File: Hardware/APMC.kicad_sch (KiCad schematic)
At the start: 161 parts, among them J1 Pin header Male 2x7 P:1.27, J10 +3.3V, J11 +3.3V, J13 +3.3V, J14 Conn_01x04, J2 USB-C, J5 Terminal 1x5 P:3.5mm, J6 Terminal 1x5 P:3.5mm, J7 Terminal 1x5 P:3.5mm, J8 Conn_01x04, J9 Conn_01x04, M1 Logo_Open_Hardware_Small, Q1 DMP6023LE, Q10 BSS123, Q2 DMP6023LE, Q3 DMP6023LE, Q4 BSS123, Q5 DMP6023LE, Q6 DMP6023LE, Q7 BSS123, Q8 DMP3056L, Q9 BSS123, U1 LMR516xx, U10 TXU0202, U12 LM74703/LM74704, U13 TPS62162DSG, U2 LCFE201202A, U3 TXU0202, U4 M95P32, U5 STM32U575CITx, U6 XTR200, U7 TPS7A2031PDBVR, U8 XTR200, U9 ADS1x2S14, X1 SiT8008Bx-7x, Y1 32.768kHz

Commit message: BOM revised
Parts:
- BT1: Notes order from Farnell, DigiKey, eBay or Aliexpress -> (none); Source (none) -> in EU order from Farnell, DigiKey, eBay or AliExpress
- BTN2, H1, H2, H3, H4, J3, J4, J8, J9, M1: now left out of the parts list
- D10: Mfg MCC: BAT46WSHE3-TP -> Diotec: BAT46WS; Mouser 833-BAT46WSHE3-TP -> 637-BAT46WS; Notes 100V, 150mA -> (none)
- D4: Alt (none) -> NXP: PZU3.6B2A,115, Vishay: NXP: BZX384B3V6-*; Mfg OnSemi: MM3Z10VST1G -> NXP: PZU3.6B2A,115; Mouser 863-MM3Z10VST1G -> 771-PZU3.6B2A,115
- D5, D9: Mfg NXP:BZT52H-B10,115 -> NXP: PDZ10BF; Mouser 2069415 -> 771-PDZ10BF
- D6: Alt BAT46WJF, BAT46WSHE3-TP, GSBAT46WS, NSR02100HT1G -> BAT46WS, BAT46WJF, BAT46WSHE3-TP, GSBAT46WS, NSR02100HT1G; Mfg MCC: BAT46WSHE3-TP -> Diotec: BAT46WS; Mouser 833-BAT46WSHE3-TP -> 637-BAT46WS; Notes 100V, 150mA -> (none)
- D8: Alt (none) -> OnSemi: MM3Z3V3ST1G, NXP: PZU3.3B2A,115; Mfg NXP: PDZ3.3B,115 -> OnSemi: MM3Z3V3ST1G; Mouser 771-PDZ33B7115 -> 863-MM3Z3V3ST1G
- Di1: value Display -> LCD 240x280 1.69"; Mfg (none) -> ?; Source Aliexpress, eBay, Allegro etc. -> e.g. https://aliexpress.com/item/1005009710952964.html, htt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
- ENC1: Bourns PEC11R-4120K-S0018 (18 dents), PEC11R-4320K-S0012 (12 dents) -> PEC11R-4215K-S0024 (24 dent), PEC11R-4315K-S0012 (12 dent); Mouser 652-PEC11R4120KS0018 -> 652-PEC11R-4215K-S24; Remarks shaft 20mm Knurled, with switch, number of dents = number o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 -> base hight 6.5mm, shaft 15mm Knurled, with switch, number o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; Remarks2 PEC11R4 requires standofs 6.5 mm -> (none); now left out of the parts list
- ENC2: Mfg CUI: RIC11-31S10K2-GSMT -> CUI: RIC11-22S11K5S-USMT; Mouser 179-RIC1131S10K2GSMT -> 179-RIC122S11K5SUSMT; Remarks (none) -> base height: 4.5, mm, shaft: 10.5mm (15 mm total); now in the parts list
- J10, J11, J13: value +3.3V -> Conn_01x03
- J12: value (none) -> Conn_02x08
- J2: value USB-C -> USB-C receptacle; Alt GCT: USB4105-GF-A, Molex: 17179-0001, AMP: 10155435-00011LF -> GCT: USB4105-GF-A-120, Molex: 17179-0001, AMP: 10155435-000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; Mfg (none) -> GCT: USB4105-GF-A; Mouser (none) -> 640-USB4105-GF-A-120
- J5, J6, J7: Alt (none) -> AdamTech: EBWA-05-A, GCT: TAD05-05-1-L-G, TE:1546551-5, Pho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; Angle55 GCT: TBD05-04-1-G-G, Phoenix: 1751112, Wurth: 691221120004,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 -> (none); Mfg Phoenix: 5430027 -> AdamTech: EBWA-05-A; Mouser 651-5430027 -> 737-EBWA-05-A; Vertical TE:1546551-4, Phoenix:5430027, Eaton: EM392304 -> (none)
- Q10, Q4, Q7, Q9: Alt (none) -> Toshiba: SSM3K7002CFU,LF, NXP: NX138BKWX, DiodesInc: DMN62D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; Mfg DiodesInc: BSS123W-7-F -> Toshiba: SSM3K7002CFU,LF; Mouser 621-BSS123W-F -> 757-SSM3K7002CFULF
- Q2, Q3, Q5, Q6: Alt (none) -> MCC: MCT090P10L-TP
- R1, R2: Mfg Yageo: RT0603DRE075K1L -> Susumu: RR0816P-512-D; Mouser 603-RT0603DRE075K1L -> 754-RR0816P-512D
- R19: Mfg Susumu: RG1608P-512-D-T5 -> Susumu: RR0816P-512-D; Mouser 754-RG1608P-512DT5 -> 754-RR0816P-512D
- R20, R27, R32, R34: R R1 -> (none)
- R28: value 300k -> 681k; Mfg Panasonic: ERA-3AEB304V -> Yageo: RT0603BRD07681KL; Mouser 667-ERA-3AEB304V -> 603-RT0603BRD07681KL
- R33: value 300k -> 1.5M; Mfg Panasonic: ERA-3AEB304V -> Vishay: MCT0603MD1504BP500; Mouser 667-ERA-3AEB304V -> 594-MCT0603MD1504BP5
- R35: value 300k -> X; Mfg Panasonic: ERA-3AEB304V -> (none); Mouser 667-ERA-3AEB304V -> (none); now not fitted; now left out of the parts list
- R42: Remarks (none) -> 1%
- R6: Mfg Yageo: RT0603DRE10100KL -> Susumu: RG1608P-104-D-T5; Mouser 603-RT0603DRE10100KL -> 754-RG1608P-104DT5
- S1, S2, S3: value Jumper_2.0 -> Shunt P: 2.0 mm
- U13: Mfg TPS62162DSGR -> TI: TPS62162DSGR
- U4: Alt2 (none) -> M95P32-IXMNT, Package_SO:SO-8_3.9x4.9mm_P1.27mm (better ava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
- U6, U8: Mfg (none) -> TI: XTR200DQCR; Mouser (none) -> 595-XTR200DQCR
- U9: Alt TI: ADS122S14 (24-bit version, pin compatible) -> 24-bit pin-compatible version TI: ADS122S14, Mouser: 595-AD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; Mfg (none) -> TI: ADS112S14IRTER; Mgf TI: ADS112S14IRTER -> (none)
- Y1: Alt (none) -> ECS-.327-CDX-1128, ECS-.327-6-34RR-TR, ECS-.327-CDX-1128, E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; Notes see ST AN2867 for more options -> refer to ST document AN2867 for more options; ST reccomended ECS-.327-CDX-1128, ECS-.327-6-34RR-TR, ECS-.327-CDX-1128, E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 -> (none)
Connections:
- net SW: now reaches C20.1, L1.1, U1.6 (SW)
- no-connect marks 10 -> 18
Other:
- note added: "AWG 16-30"
- note added: "Select R21, R28, R33, and R35 according to the required input range. E.g. use a 300 kΩ, 681 kΩ, or 1.5 MΩ resistor for the 65 V, 30 V, and 15 V ranges, respectively."
- note removed: "Select R21, R28, R33, and R35 according to the required input range. E.g. use a 300 kΩ, 681 kΩ, or 2.5 MΩ resistor for the 65 V, 30 V, and 10 V ranges, respectively."
- moved on the sheet: C18, C46, D10, D13, J6, Q6, R17, R38, R40, U8

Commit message: schematic fix
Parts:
- Q1: symbol Transistor_FET:ZXMP4A16G -> Transistor_FET:BSP89; Alt MCC: MCT090P10L-TP -> TSMC: TSM950N10CW RPG; Mfg DiodesInc: DMP6023LE-13 -> OnSemi: FDT86102LZ; Mouser 621-DMP6023LE-13 -> 512-FDT86102LZ; Remarks any P-CH SOT-223-3 Mosfet with Vgs(th)max<2V, Vds>60V, Id>5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 -> any N-CH SOT-223-3 Mosfet with Vgs(th)max<2V, Vds>70V, Id>5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
- Q8: Note (none) -> consider using LM66100 in SC-70-6 pkg instead
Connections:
- net VCC: now also Q1.2 (D); no longer Q1.3 (S)
- net VIN: now also Q1.3 (S); no longer Q1.2 (D)
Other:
- moved on the sheet: Q1
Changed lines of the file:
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@@
 			)
 		)
-		(property "Angle55" ""
-			(at 106.68 30.48 0)
-			(hide yes)
-			(show_name no)
-			(do_not_autoplace no)
-			(effects
-				(font
-					(size 1.27 1.27)
-				)
-			)
-		)
-		(property "Vertical" ""
-			(at 106.68 30.48 0)
-			(hide yes)
-			(show_name no)
-			(do_not_autoplace no)
-			(effects
-				(font
-					(size 1.27 1.27)
-				)
-			)
-		)
-		(property "AliExpress" ""
-			(at 106.68 30.48 0)
-			(hide yes)
-			(show_name no)
-			(do_not_autoplace no)
-			(effects
-				(font
-					(size 1.27 1.27)
-				)
-			)
-		)
-		(property "Source" ""
-			(at 106.68 30.48 0)
-			(hide yes)
-			(show_name no)
-			(do_not_autoplace no)
-			(effects
-				(font
-					(size 1.27 1.27)
-				)
-			)
-		)
-		(property "ST reccomended" ""
+		(property "Note" "consider using LM66100 in SC-70-6 pkg instead"
 			(at 106.68 30.48 0)
 			(hide yes)
@@
 	)
 	(symbol
-		(lib_id "Transistor_FET:ZXMP4A16G")
-		(at 33.02 27.94 90)
+		(lib_id "Transistor_FET:BSP89")
+		(at 33.02 27.94 270)
+		(mirror x)
 		(unit 1)
 		(body_style 1)
@@
 		(dnp no)
 		(property "Reference" "Q1"
-			(at 36.576 29.21 90)
+			(at 35.052 28.956 90)
 			(show_name no)
 			(do_not_autoplace no)
@@
 					(size 1.27 1.27)
 				)
+				(justify left)
 			)
 		)
@@
 		)
 		(property "Footprint" "Package_TO_SOT_SMD:SOT-223-3_TabPin2"
-			(at 34.925 22.86 0)
+			(at 31.115 22.86 0)
 			(hide yes)
 			(show_name no)
@@
 		)
 		(property "Datasheet" ""
-			(at 33.02 27.94 0)
+			(at 29.21 22.86 0)
 			(hide yes)
 			(show_name no)
@@
 			)
 		)
-		(property "Mouser" "621-DMP6023LE-13"
+		(property "Mouser" "512-FDT86102LZ"
 			(at 33.02 27.94 0)
 			(hide yes)
@@
 			)
 		)
-		(property "Mfg" "DiodesInc: DMP6023LE-13"
+		(property "Mfg" "OnSemi: FDT86102LZ"
 			(at 33.02 27.94 0)
 			(hide yes)
@@
 			)
 		)
-		(property "Remarks" "any P-CH SOT-223-3 Mosfet with Vgs(th)max<2V, Vds>60V, Id>5A, low Rds(on)"
+		(property "Remarks" "any N-CH SOT-223-3 Mosfet with Vgs(th)max<2V, Vds>70V, Id>5A, low Rds(on)"
 			(at 33.02 27.94 90)
 			(hide yes)
@@
 			)
 		)
-		(property "Alt" "MCC: MCT090P10L-TP"
+		(property "Alt" "TSMC: TSM950N10CW RPG"
 			(at 33.02 27.94 90)
 			(hide yes)

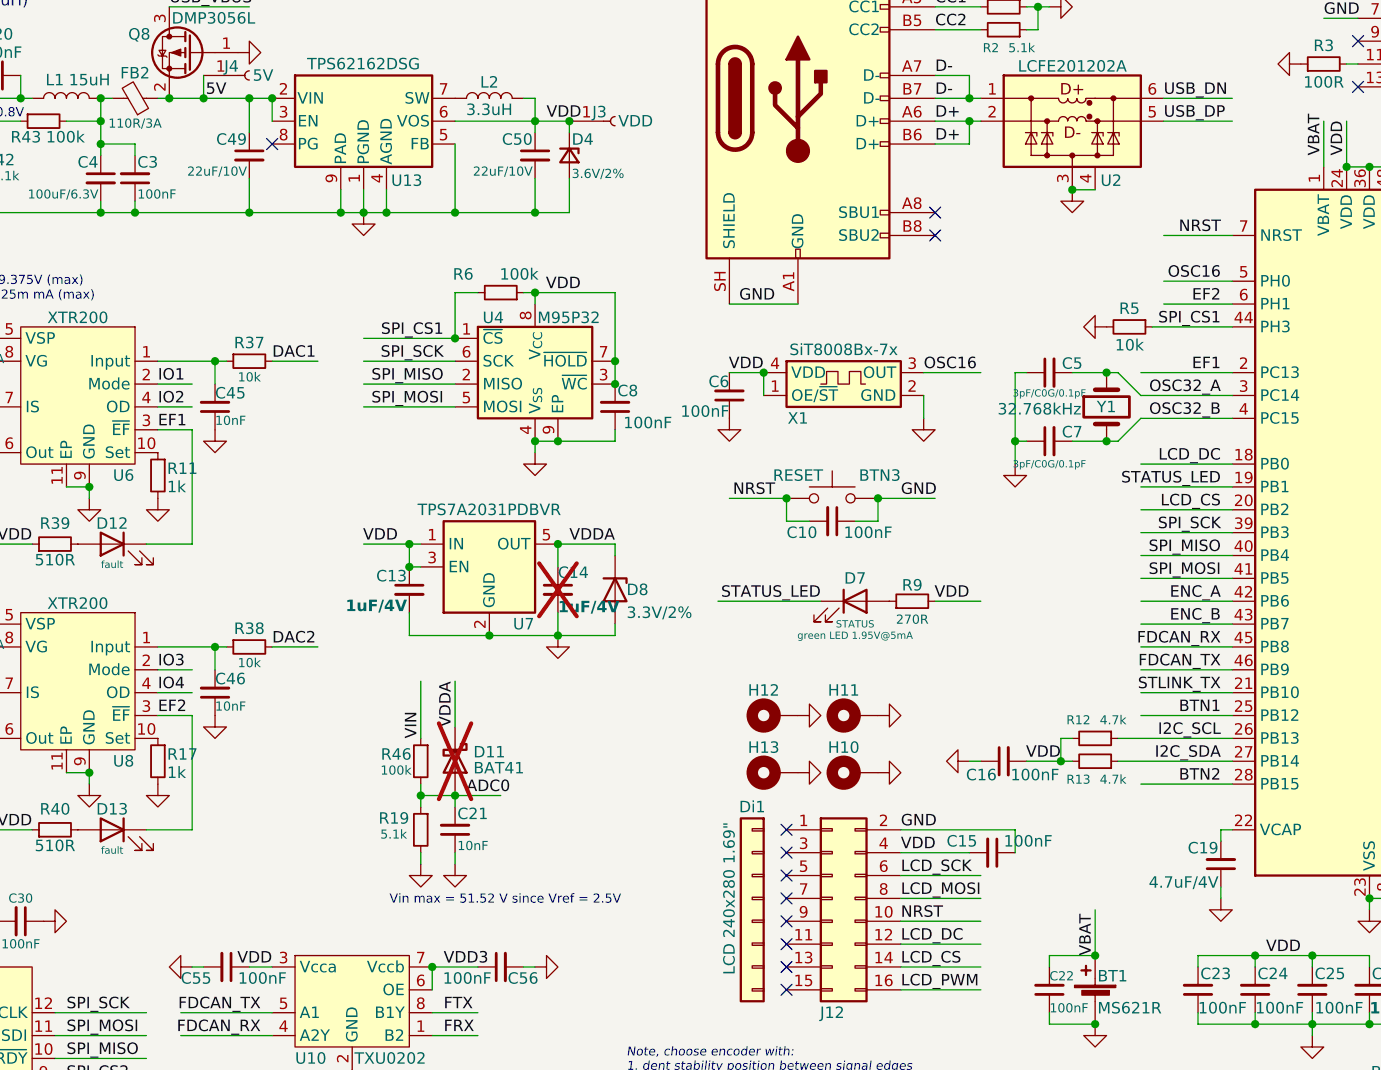
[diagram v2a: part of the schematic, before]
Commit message: R19 fix
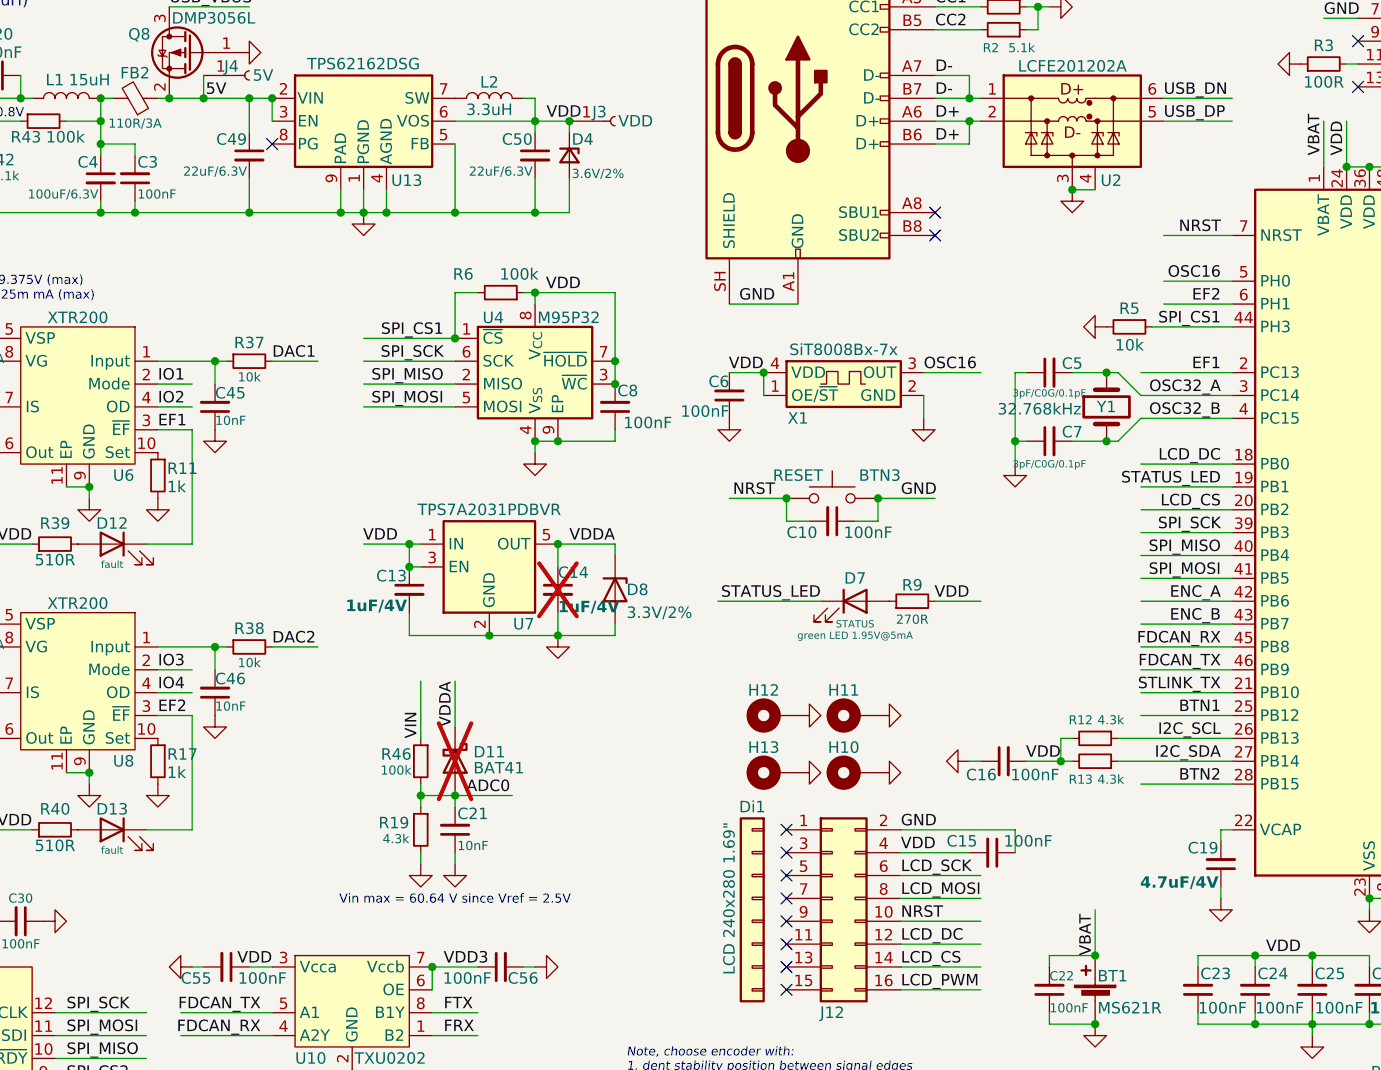
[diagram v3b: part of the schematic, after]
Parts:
- C49, C50: value 22uF/10V -> 22uF/6.3V
- Q10, Q9: Notes Vds 80V min, Vgs(th) ~1.5V, Rds(on) ≤ 10Ω -> Vds(max) ≥ 30V, Vgs(th) ~1.5V, Vgs(max) ≥ ±20V, Rds(on) ≤ 1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
- R12, R13: value 4.7k -> 4.3k; Mfg Susumu: RG1608P-472-D-T5 -> Susumu: RR0816P-432-D; Mouser 754-RG1608P-472DT5 -> 754-RR0816P-432D
- R19: value 5.1k -> 4.3k; Mfg Susumu: RR0816P-512-D -> Susumu: RR0816P-432-D; Mouser 754-RR0816P-512D -> 754-RR0816P-432D
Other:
- note added: "Vin max = 60.64 V since Vref = 2.5V"
- note removed: "Vin max = 51.52 V since Vref = 2.5V"
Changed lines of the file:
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@@
 		)
 	)
-	(text "Vin max = 51.52 V since Vref = 2.5V"
+	(text "Vin max = 60.64 V since Vref = 2.5V"
 		(exclude_from_sim no)
-		(at 141.478 124.714 0)
+		(at 135.89 124.714 0)
 		(effects
 			(font
@@
 	(wire
 		(pts
-			(xy 135.89 113.03) (xy 140.97 113.03)
+			(xy 135.89 113.03) (xy 142.24 113.03)
 		)
 		(stroke
@@
 		(dnp no)
 		(property "Reference" "R19"
-			(at 130.81 115.57 0)
+			(at 130.81 116.078 0)
 			(show_name no)
 			(do_not_autoplace no)
@@
 			)
 		)
-		(property "Value" "5.1k"
-			(at 130.556 117.348 0)
+		(property "Value" "4.3k"
+			(at 130.81 117.856 0)
 			(show_name no)
 			(do_not_autoplace no)
@@
 			)
 		)
-		(property "Mfg" "Susumu: RR0816P-512-D"
+		(property "Mfg" "Susumu: RR0816P-432-D"
 			(at 132.08 116.84 0)
 			(hide yes)
@@
 			)
 		)
-		(property "Mouser" "754-RR0816P-512D"
+		(property "Mouser" "754-RR0816P-432D"
 			(at 132.08 116.84 0)
 			(hide yes)
@@
 			)
 		)
-		(property "Value" "22uF/10V"
+		(property "Value" "22uF/6.3V"
 			(at 144.526 43.688 0)
 			(show_name no)
@@
 		(dnp no)
 		(property "Reference" "R13"
-			(at 206.502 111.252 90)
+			(at 206.756 111.252 90)
 			(show_name no)
 			(do_not_autoplace no)
@@
 			)
 		)
-		(property "Value" "4.7k"
-			(at 207.518 111.252 90)
+		(property "Value" "4.3k"
+			(at 207.264 111.252 90)
 			(show_name no)
 			(do_not_autoplace no)
@@
 			)
 		)
-		(property "Mfg" "Susumu: RG1608P-472-D-T5"
+		(property "Mfg" "Susumu: RR0816P-432-D"
 			(at 207.01 109.22 0)
 			(hide yes)
@@
 			)
 		)
-		(property "Mouser" "754-RG1608P-472DT5"
+		(property "Mouser" "754-RR0816P-432D"
 			(at 207.01 109.22 0)
 			(hide yes)
@@
 		(dnp no)
 		(property "Reference" "R12"
-			(at 206.502 104.648 90)
+			(at 206.756 104.648 90)
 			(show_name no)
 			(do_not_autoplace no)
@@
 			)
 		)
-		(property "Value" "4.7k"
-			(at 207.518 104.648 90)
+		(property "Value" "4.3k"
+			(at 207.264 104.648 90)
 			(show_name no)
 			(do_not_autoplace no)
@@
 			)
 		)
-		(property "Mfg" "Susumu: RG1608P-472-D-T5"
+		(property "Mfg" "Susumu: RR0816P-432-D"
 			(at 207.01 106.68 0)
 			(hide yes)
@@
 			)
 		)
-		(property "Mouser" "754-RG1608P-472DT5"
+		(property "Mouser" "754-RR0816P-432D"
 			(at 207.01 106.68 0)
 			(hide yes)
@@
 			)
 		)
-		(property "Notes" "Vds 80V min, Vgs(th) ~1.5V, Rds(on) ≤ 10Ω"
+		(property "Notes" "Vds(max) ≥ 30V, Vgs(th) ~1.5V, Vgs(max) ≥ ±20V, Rds(on) ≤ 10Ω"
 			(at 95.25 172.72 0)
 			(hide yes)
@@
 			)
 		)
-		(property "Angle55" ""
-			(at 95.25 172.72 90)
-			(hide yes)
-			(show_name no)
-			(do_not_autoplace no)
-			(effects
-				(font
-					(size 1.27 1.27)
-				)
-			)
-		)
-		(property "Vertical" ""
-			(at 95.25 172.72 90)
-			(hide yes)
-			(show_name no)
-			(do_not_autoplace no)
-			(effects
-				(font
-					(size 1.27 1.27)
-				)
-			)
-		)
-		(property "AliExpress" ""
-			(at 95.25 172.72 90)
-			(hide yes)
-			(show_name no)
-			(do_not_autoplace no)
-			(effects
-				(font
-					(size 1.27 1.27)
-				)
-			)
-		)
-		(property "Source" ""
-			(at 95.25 172.72 90)
-			(hide yes)
-			(show_name no)
-			(do_not_autoplace no)
-			(effects
-				(font
-					(size 1.27 1.27)
-				)
-			)
-		)
-		(property "ST reccomended" ""
-			(at 95.25 172.72 90)
-			(hide yes)
-			(show_name no)
-			(do_not_autoplace no)
-			(effects
-				(font
-					(size 1.27 1.27)
-				)
-			)
-		)
 		(property "Alt" "Toshiba: SSM3K7002CFU,LF, NXP: NX138BKWX, DiodesInc: DMN62D0UWQ-7, MCC: 2N7002KW-TP, DiodesInc: BSS123W-7-F, OnSemi: 2N7002KW"
 			(at 95.25 172.72 90)
@@
 				(font
 					(size 1.27 1.27)
+					(thickness 0.254)
+					(bold yes)
+					(color 132 0 132 1)
 				)
 				(justify left)
@@
 			)
 		)
-		(property "Notes" "Vds 80V min, Vgs(th) ~1.5V, Rds(on) ≤ 10Ω"
+		(property "Notes" "Vds(max) ≥ 30V, Vgs(th) ~1.5V, Vgs(max) ≥ ±20V, Rds(on) ≤ 10Ω"
 			(at 88.9 177.8 0)
 			(hide yes)
@@
 			)
 		)
-		(property "Angle55" ""
-			(at 88.9 177.8 90)
-			(hide yes)
-			(show_name no)
-			(do_not_autoplace no)
-			(effects
-				(font
-					(size 1.27 1.27)
-				)
-			)
-		)
-		(property "Vertical" ""
-			(at 88.9 177.8 90)
-			(hide yes)
-			(show_name no)
-			(do_not_autoplace no)
-			(effects
-				(font
-					(size 1.27 1.27)
-				)
-			)
-		)
-		(property "AliExpress" ""
-			(at 88.9 177.8 90)
-			(hide yes)
-			(show_name no)
-			(do_not_autoplace no)
-			(effects
-				(font
-					(size 1.27 1.27)
-				)
-			)
-		)
-		(property "Source" ""
-			(at 88.9 177.8 90)
-			(hide yes)
-			(show_name no)
-			(do_not_autoplace no)
-			(effects
-				(font
-					(size 1.27 1.27)
-				)
-			)
-		)
-		(property "ST reccomended" ""
-			(at 88.9 177.8 90)
-			(hide yes)
-			(show_name no)
-			(do_not_autoplace no)
-			(effects
-				(font
-					(size 1.27 1.27)
-				)
-			)
-		)
 		(property "Alt" "Toshiba: SSM3K7002CFU,LF, NXP: NX138BKWX, DiodesInc: DMN62D0UWQ-7, MCC: 2N7002KW-TP, DiodesInc: BSS123W-7-F, OnSemi: 2N7002KW"
 			(at 88.9 177.8 90)
@@
 			)
 		)
-		(property "Value" "22uF/10V"
+		(property "Value" "22uF/6.3V"
 			(at 112.776 43.688 0)
 			(show_name no)

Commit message: label fix
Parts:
- J10, J11, J13: Label 3V 5V -> 3.3V 5V
- J3: Label VDD -> 3.3V
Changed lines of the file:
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@@
 			)
 		)
-		(property "Label" "3V 5V"
+		(property "Label" "3.3V 5V"
 			(at 114.046 153.67 0)
 			(hide yes)
@@
 			)
 		)
-		(property "Label" "3V 5V"
+		(property "Label" "3.3V 5V"
 			(at 124.206 193.04 0)
 			(hide yes)
@@
 			)
 		)
-		(property "Label" "VDD"
+		(property "Label" "3.3V"
 			(at 155.956 38.1 0)
 			(show_name no)
@@
 			)
 		)
-		(property "Label" "3V 5V"
+		(property "Label" "3.3V 5V"
 			(at 92.456 193.04 0)
 			(hide yes)

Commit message: post-prod updates
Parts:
- removed C31, C36, C38, C43: 10nF, Custom:C_0603_1608Metric_Pad0.98x0.95mm_HandSolder, symbol Device:C_Small
- removed C52: 100nF, Capacitor_SMD:C_0603_1608Metric_Pad1.08x0.95mm_HandSolder, symbol Device:C_Small
- removed C57: 100nF, Custom:C_0603_1608Metric_Pad0.98x0.95mm_HandSolder, symbol Device:C_Small
- removed Q10, Q9: BSS123, Package_TO_SOT_SMD:SOT-323_SC-70, symbol Transistor_FET:AO3400A
- removed R16, R41: 3.3k, Resistor_SMD:R_0603_1608Metric_Pad0.98x0.95mm_HandSolder, symbol Device:R_Small
- added C33: 10nF, Custom:RC_Array_Isolated_4_0805, symbol RC_Arrays:C_Array_04_Isolated
- added C58: 100nF, Capacitor_SMD:C_0603_1608Metric_Pad1.08x0.95mm_HandSolder, symbol Device:C_Small
- added R24, R25: 3.3k, Resistor_SMD:R_0603_1608Metric_Pad0.98x0.95mm_HandSolder, symbol Device:R_Small
- added R29: 100k, Resistor_SMD:R_0603_1608Metric_Pad0.98x0.95mm_HandSolder, symbol Device:R_Small
- added U11: PCA9306, Custom:VSSOP-8_2.3x2mm_P0.5mm, symbol PCA9306:PCA9306
- H1, H2, H3, H4: value MountingHole -> M2.5x7; Alt (none) -> Harwin: R25-1000702, Wurth: 970070151, 970070154, 970070155; Mfg (none) -> Harwin: R25-1000702; Mouser (none) -> 855-R25-1000702; now in the parts list
- R21, R28, R33, R35: footprint Resistor_SMD:R_0603_1608Metric_Pad0.98x0.95mm_HandSolder -> Resistor_SMD:R_0805_2012Metric
- U4: footprint Custom:DFN-8-1EP_4x4mm_P0.8mm_EP2.2x3.2mm -> Package_SO:SO-8_3.9x4.9mm_P1.27mm; symbol M95P32:M95P32 -> M95P32:M95P32-N; Alt2 M95P32-IXMNT, Package_SO:SO-8_3.9x4.9mm_P1.27mm (better ava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 -> (none); Mfg ST: M95P32-IXMGT/E -> ST: M95P32-IXMNT/E; Mouser 511-M95P32-IXMGT/E -> 511-M95P32-IXMNT/E; Note there is smaller WLCSP8 (2.6x1.5 mm) package available -> smaller packages available (WLCSP8 2.6x1.5 mm and DFN-8 4x4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
- U9: footprint Package_DFN_QFN:WQFN-16-1EP_3x3mm_P0.5mm_EP1.68x1.68mm_ThermalVias -> Custom:WQFN-16-1EP_3x3mm_P0.5mm_EP1.68x1.68mm_ThermalVias
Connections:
- net ADC1: now also C33.1 (C1.1)
- net ADC2: now also C33.2 (C2.1)
- net ADC3: now also C33.3 (C3.1)
- net ADC4: now also C33.4 (C4.1)
- net GND: now also C33.5 (C4.2), C33.6 (C3.2), C33.7 (C2.2), C33.8 (C1.2), C58.2, U11.1 (GND); no longer U4.9 (EP)
- net I2C_SCL: now also U11.3 (SCL1)
- net I2C_SDA: now also U11.4 (SDA1)
- net SCL: now also R24.1, U11.6 (SCL2)
- net SDA: now also R25.1, U11.5 (SDA2)
- net VDD: now also C58.1, U11.2 (V1)
- net VDD1: now also R24.2, R25.2, R29.2
- new net: R29.1, U11.7 (V2), U11.8 (EN)
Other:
- moved on the sheet: C41, C42, C51, C53, C54, C55, C56, C8, J10, J11, J13, J14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
